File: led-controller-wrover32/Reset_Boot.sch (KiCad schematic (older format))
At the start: 8 parts, among them Q5 BSS138DW-7-F, SW1 SW_SPST_KMR2, SW2 SW_SPST_KMR2

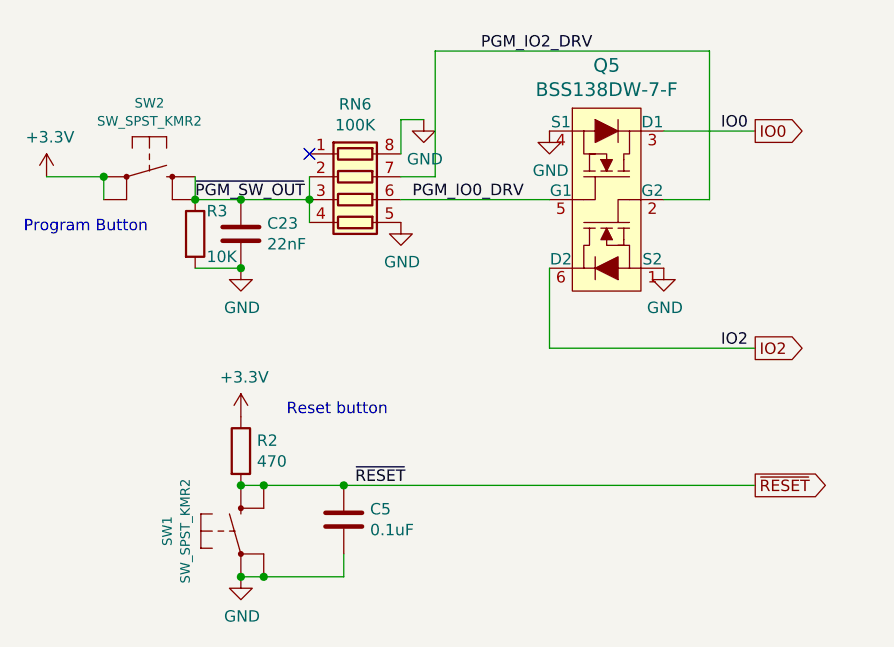
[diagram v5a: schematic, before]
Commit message: Multiple changes from v3.7
1. Fixed microphone so it uses the left channel
2. Reduced the number of unique components, i.e. replacing a couple of
   resistor networks with already used resistors
3. Removed unneeded resistor in programming circuit
4. Moved speaker chip to the other side to be closer to the connector
5. Cleaned up some of the traces and removed some inner-layer traces.
6. Moved reset switch to the edge to make access easier.
7. Added big via to line up with daughter card.
8. Replaced BSS138 transistor array with two BSS138 transistors to reduce
   the unique component count and reduce cost.

Signed-off-by: Aaron Williams <aaron.w2@gmail.com>
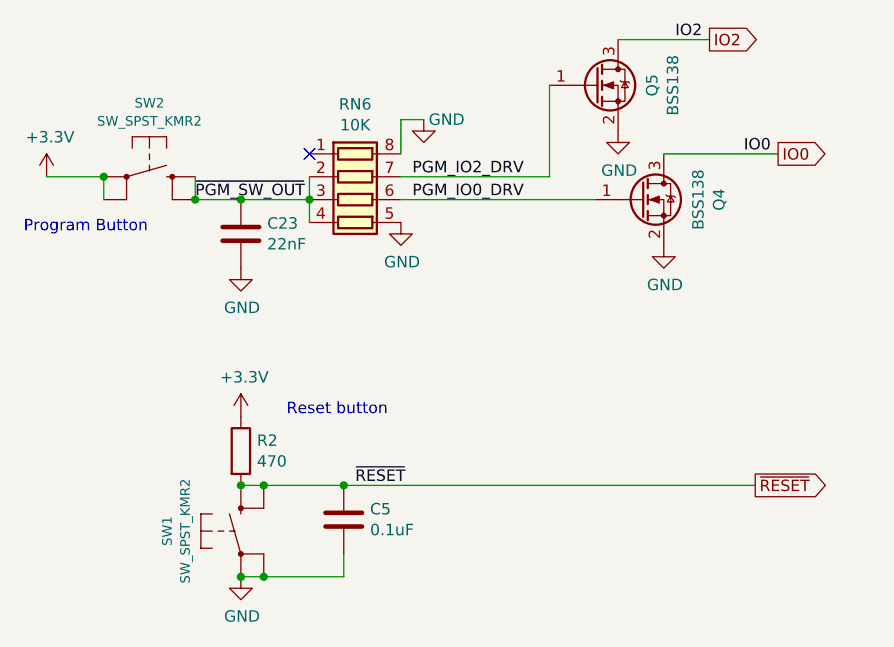
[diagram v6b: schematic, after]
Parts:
- removed Q5: BSS138DW-7-F, Package_TO_SOT_SMD:SOT-363_SC-70-6, symbol dk_Transistors-FETs-MOSFETs-Arrays:BSS138DW-7-F
- removed R3: 10K, Resistor_SMD:R_0603_1608Metric, symbol Device:R
- added Q4, Q5: BSS138, Package_TO_SOT_SMD:SOT-23, symbol Transistor_FET:BSS138
- C5: SPURL - -> https://www.digikey.com/product-detail/en/murata-electronic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
- R2: SPURL - -> https://www.digikey.com/products/en?keywords=1276-4619-1-ND
- RN6: value 100K -> 10K; DESC RES ARRAY 4 RES 100K OHM 1206 -> RES ARRAY 4 RES 10K OHM 1206; MPN EXB-V8V104JV -> EXB-V8V103JV; SPN Y4104CT-ND -> Y4103CT-ND; SPURL https://www.digikey.com/product-detail/en/bourns-inc/CAT16-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 -> https://www.digikey.com/products/en?keywords=Y4103CT-ND
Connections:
- net GND: now also Q4.2 (S), Q5.2 (S)
- net IO0: now also Q4.3 (D)
- net IO2: now also Q5.3 (D)
- net PGM_IO0_DRV: now also Q4.1 (G)
- net PGM_IO2_DRV: now also Q5.1 (G)
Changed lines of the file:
@@
 $EndDescr
-$Comp
-L dk_Transistors-FETs-MOSFETs-Arrays:BSS138DW-7-F Q5
-U 1 1 5DD66E94
-P 5050 2350
-F 0 "Q5" H 5000 2837 60  0000 C CNN
-F 1 "BSS138DW-7-F" H 5000 2731 60  0000 C CNN
-F 2 "Package_TO_SOT_SMD:SOT-363_SC-70-6" H 5250 2550 60  0001 L CNN
-F 3 "https://www.diodes.com/assets/Datasheets/ds30203.pdf" V 5250 2650 60  0001 L CNN
-F 4 "BSS138DW-FDICT-ND" H 5250 2750 60  0001 L CNN "Digi-Key_PN"
-F 5 "BSS138DW-7-F" H 5250 2850 60  0001 L CNN "MPN"
-F 6 "Discrete Semiconductor Products" H 5250 2950 60  0001 L CNN "Category"
-F 7 "Transistors - FETs, MOSFETs - Arrays" H 5250 3050 60  0001 L CNN "Family"
-F 8 "https://www.diodes.com/assets/Datasheets/ds30203.pdf" H 5250 3150 60  0001 L CNN "DK_Datasheet_Link"
-F 9 "/product-detail/en/diodes-incorporated/BSS138DW-7-F/BSS138DW-FDICT-ND/808541" H 5250 3250 60  0001 L CNN "DK_Detail_Page"
-F 10 "MOSFET 2N-CH 50V 0.2A SC70-6" H 5250 3350 60  0001 L CNN "Description"
-F 11 "Diodes Incorporated" H 5250 3450 60  0001 L CNN "Manufacturer"
-F 12 "Active" H 5250 3550 60  0001 L CNN "Status"
-F 13 "Diodes Incorporated" H 5050 2350 50  0001 C CNN "MFR"
-F 14 "Digikey" H 5050 2350 50  0001 C CNN "SPR"
-F 15 "BSS138DW-FDICT-ND" H 5050 2350 50  0001 C CNN "SPN"
-F 16 "https://www.digikey.com/products/en/discrete-semiconductor-products/transistors-fets-mosfets-arrays/289?k=BSS138DW-7-F&k=&pkeyword=BSS138DW-7-F&sv=0&pv7=2&sf=0&quantity=&ColumnSort=0&page=1&stock=1&nstock=1&pageSize=500" H 5050 2350 50  0001 C CNN "SPURL"
-F 17 "MOSFET 2N-CH 50V 0.2A SC70-6" H 0   0   50  0001 C CNN "DESC"
-	1    5050 2350
-	1    0    0    -1
-$EndComp
 $Comp
 L switch_tact_smt:SW_SPST_KMR2 SW2
@@
 L power:GND #PWR0127
 U 1 1 5DD73FDE
-P 4750 2150
-F 0 "#PWR0127" H 4750 1900 50  0001 C CNN
-F 1 "GND" H 4755 1977 50  0000 C CNN
-F 2 "" H 4750 2150 50  0001 C CNN
-F 3 "" H 4750 2150 50  0001 C CNN
-	1    4750 2150
-	1    0    0    -1
-$EndComp
-$Comp
-L power:GND #PWR0128
-U 1 1 5DD74502
-P 5250 2750
-F 0 "#PWR0128" H 5250 2500 50  0001 C CNN
-F 1 "GND" H 5255 2577 50  0000 C CNN
-F 2 "" H 5250 2750 50  0001 C CNN
-F 3 "" H 5250 2750 50  0001 C CNN
-	1    5250 2750
+P 5250 2650
+F 0 "#PWR0127" H 5250 2400 50  0001 C CNN
+F 1 "GND" H 5255 2477 50  0000 C CNN
+F 2 "" H 5250 2650 50  0001 C CNN
+F 3 "" H 5250 2650 50  0001 C CNN
+	1    5250 2650
 	1    0    0    -1
 $EndComp
@@
 P 3900 2450
 F 0 "RN6" V 3483 2450 50  0000 C CNN
-F 1 "100K" V 3574 2450 50  0000 C CNN
+F 1 "10K" V 3574 2450 50  0000 C CNN
 F 2 "Resistor_SMD:R_Array_Convex_4x0603" V 4175 2450 50  0001 C CNN
 F 3 "https://industrial.panasonic.com/cdbs/www-data/pdf/AOC0000/AOC0000C14.pdf" H 3900 2450 50  0001 C CNN
 F 4 "Panasonic" H 3900 2450 50  0001 C CNN "MFR"
-F 5 "EXB-V8V104JV" H 3900 2450 50  0001 C CNN "MPN"
+F 5 "EXB-V8V103JV" H 3900 2450 50  0001 C CNN "MPN"
 F 6 "Digikey" H 3900 2450 50  0001 C CNN "SPR"
-F 7 "Y4104CT-ND" H 3900 2450 50  0001 C CNN "SPN"
-F 8 "https://www.digikey.com/product-detail/en/bourns-inc/CAT16-1003F4LF/CAT16-1003F4LFCT-ND/3592894" H 3900 2450 50  0001 C CNN "SPURL"
-F 9 "RES ARRAY 4 RES 100K OHM 1206" H 0   0   50  0001 C CNN "DESC"
+F 7 "Y4103CT-ND" H 3900 2450 50  0001 C CNN "SPN"
+F 8 "https://www.digikey.com/products/en?keywords=Y4103CT-ND" H 3900 2450 50  0001 C CNN "SPURL"
+F 9 "RES ARRAY 4 RES 10K OHM 1206" H 0   0   50  0001 C CNN "DESC"
 	1    3900 2450
 	0    1    1    0
@@
 F 6 "Digikey" H -1100 2500 50  0001 C CNN "SPR"
 F 7 "1276-4619-1-ND" H -1100 2500 50  0001 C CNN "SPN"
-F 8 "-" H -1100 2500 50  0001 C CNN "SPURL"
+F 8 "https://www.digikey.com/products/en?keywords=1276-4619-1-ND" H -1100 2500 50  0001 C CNN "SPURL"
 F 9 "RES SMD 470 OHM 1% 1/10W 0603" H 0   0   50  0001 C CNN "DESC"
 	1    3400 3550
@@
 F 6 "Digikey" H -1100 2300 50  0001 C CNN "SPR"
 F 7 "490-4779-1-ND" H -1100 2300 50  0001 C CNN "SPN"
-F 8 "-" H -1100 2300 50  0001 C CNN "SPURL"
+F 8 "https://www.digikey.com/product-detail/en/murata-electronics/GCM188R71H104KA57D/490-4779-1-ND/1641698" H -1100 2300 50  0001 C CNN "SPURL"
 F 9 "CAP CER 0.1UF 50V X7R 0603" H 0   0   50  0001 C CNN "DESC"
 	1    3850 3850
@@
 $EndComp
 $Comp
-L Device:R R3
-U 1 1 5DBEA787
-P 3200 2600
-F 0 "R3" H 3250 2700 50  0000 L CNN
-F 1 "10K" H 3250 2500 50  0000 L CNN
-F 2 "Resistor_SMD:R_0603_1608Metric" V 3130 2600 50  0001 C CNN
-F 3 "http://www.vishay.com/docs/20035/dcrcwe3.pdf" H 3200 2600 50  0001 C CNN
-F 4 "Vishay Dale" H 0   0   50  0001 C CNN "MFR"
-F 5 "CRCW060310K0FKEC" H 0   0   50  0001 C CNN "MPN"
-F 6 "Digikey" H 0   0   50  0001 C CNN "SPR"
-F 7 "541-2979-1-ND" H 0   0   50  0001 C CNN "SPN"
-F 8 "-" H 0   0   50  0001 C CNN "SPURL"
-F 9 "RES SMD 10K OHM 1% 1/10W 0603" H 0   0   50  0001 C CNN "DESC"
-	1    3200 2600
-	1    0    0    -1
-$EndComp
-$Comp
 L power:GND #PWR0135
 U 1 1 5E105B99
 P 4200 2100
 F 0 "#PWR0135" H 4200 1850 50  0001 C CNN
-F 1 "GND" H 4205 1927 50  0000 C CNN
+F 1 "GND" H 4300 2100 50  0000 C CNN
 F 2 "" H 4200 2100 50  0001 C CNN
 F 3 "" H 4200 2100 50  0001 C CNN
@@
 	1    0    0    -1
 $EndComp
-Text Label 5500 2150 0    50   ~ 0
+$Comp
+L Transistor_FET:BSS138 Q4
+U 1 1 5EC189C0
+P 5150 2450
+F 0 "Q4" V 5492 2450 50  0000 C CNN
+F 1 "BSS138" V 5401 2450 50  0000 C CNN
+F 2 "Package_TO_SOT_SMD:SOT-23" H 5350 2375 50  0001 L CIN
+F 3 "https://www.fairchildsemi.com/datasheets/BS/BSS138.pdf" H 5150 2450 50  0001 L CNN
+F 4 "ON Semiconductor" H 5150 2450 50  0001 C CNN "MFR"
+F 5 "BSS138" H 5150 2450 50  0001 C CNN "MPN"
+F 6 "Digikey" H 5150 2450 50  0001 C CNN "SPR"
+F 7 "BSS138CT-ND" H 5150 2450 50  0001 C CNN "SPN"
+F 8 "https://www.digikey.com/product-detail/en/on-semiconductor/BSS138/BSS138CT-ND/244294" H 5150 2450 50  0001 C CNN "SPURL"
+F 9 "N-Channel 50V 220mA (Ta) 360mW (Ta) Surface Mount SOT-23-3" H 0   0   50  0001 C CNN "DESC"
+	1    5150 2450
+	1    0    0    -1
+$EndComp
+$Comp
+L Transistor_FET:BSS138 Q5
+U 1 1 5EC114C9
+P 4950 1950
+F 0 "Q5" V 5199 1950 50  0000 C CNN
+F 1 "BSS138" V 5290 1950 50  0000 C CNN
+F 2 "Package_TO_SOT_SMD:SOT-23" H 5150 1875 50  0001 L CIN
+F 3 "https://www.fairchildsemi.com/datasheets/BS/BSS138.pdf" H 4950 1950 50  0001 L CNN
+F 4 "ON Semiconductor" H 4950 1950 50  0001 C CNN "MFR"
+F 5 "BSS138" H 4950 1950 50  0001 C CNN "MPN"
+F 6 "Digikey" H 4950 1950 50  0001 C CNN "SPR"
+F 7 "BSS138CT-ND" H 4950 1950 50  0001 C CNN "SPN"
+F 8 "https://www.digikey.com/product-detail/en/on-semiconductor/BSS138/BSS138CT-ND/244294" H 4950 1950 50  0001 C CNN "SPURL"
+F 9 "N-Channel 50V 220mA (Ta) 360mW (Ta) Surface Mount SOT-23-3" H 0   0   50  0001 C CNN "DESC"
+	1    4950 1950
+	1    0    0    -1
+$EndComp
+$Comp
+L power:GND #PWR0128
+U 1 1 5DD74502
+P 5050 2150
+F 0 "#PWR0128" H 5050 1900 50  0001 C CNN
+F 1 "GND" H 5055 1977 50  0000 C CNN
+F 2 "" H 5050 2150 50  0001 C CNN
+F 3 "" H 5050 2150 50  0001 C CNN
+	1    5050 2150
+	1    0    0    -1
+$EndComp
+Text Label 5600 2250 0    50   ~ 0
 IO0
-Text Label 5500 3100 0    50   ~ 0
+Text Label 5300 1750 0    50   ~ 0
 IO2
-Text GLabel 5650 2150 2    50   Output ~ 0
+Text GLabel 5750 2250 2    50   Output ~ 0
 IO0
-Text GLabel 5650 3100 2    50   Output ~ 0
+Text GLabel 5450 1750 2    50   Output ~ 0
 IO2
 Text GLabel 5650 3700 2    50   Output ~ 0
@@
 Text Label 3200 2450 0    50   ~ 0
 ~PGM_SW_OUT
-Text Label 4450 1800 0    50   ~ 0
+Text Label 4150 2350 0    50   ~ 0
 PGM_IO2_DRV
 Text Label 4150 2450 0    50   ~ 0
@@
 	3700 2450 3700 2550
 Wire Wire Line
-	4100 2450 4750 2450
-Wire Wire Line
-	4100 2350 4250 2350
-Wire Wire Line
-	4250 2350 4250 1800
-Wire Wire Line
-	4250 1800 5450 1800
-Wire Wire Line
-	5450 1800 5450 2450
-Wire Wire Line
-	5450 2450 5250 2450
-Wire Wire Line
-	5250 2150 5650 2150
-Wire Wire Line
-	4750 2750 4750 3100
-Wire Wire Line
-	4750 3100 5650 3100
-Wire Wire Line
 	3850 4000 3850 4100
 Wire Wire Line
@@
 	3400 4100 3500 4100
 Wire Wire Line
-	3200 2750 3400 2750
-Wire Wire Line
 	4200 2100 4100 2100
 Wire Wire Line
 	4100 2100 4100 2250
+Wire Wire Line
+	5050 1750 5450 1750
+Wire Wire Line
+	4100 2450 4950 2450
+Wire Wire Line
+	5250 2250 5750 2250
+Wire Wire Line
+	4100 2350 4750 2350
+Wire Wire Line
+	4750 1950 4750 2350
 Connection ~ 2800 2350
 Connection ~ 3200 2450
@@
 Connection ~ 3400 4100
 Connection ~ 3500 4100
-Connection ~ 3400 2750
 NoConn ~ 3700 2250
 $EndSCHEMATC
